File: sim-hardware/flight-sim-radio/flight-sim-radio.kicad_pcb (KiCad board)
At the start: 2 copper layers, 180.5 x 50 mm, 22 parts, among them J1 Conn_01x04, J2 Conn_01x03, J3 Conn_01x08, SW1 SW_Push, SW2 SW_Rotary_1x7_MP, SW3 RotaryEncoder_Switch, SW4 RotaryEncoder_Switch, U1 74LS148, U4 TM1637, U5 TM1637

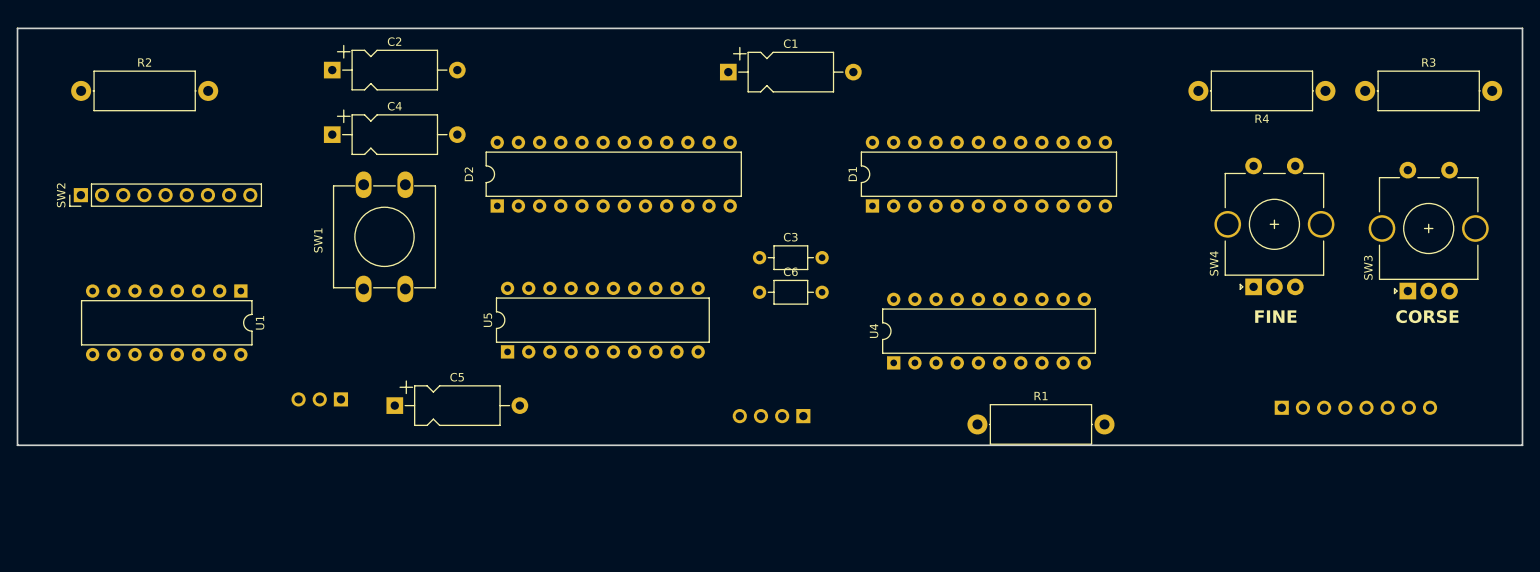
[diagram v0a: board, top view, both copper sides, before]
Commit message: 7 Segment Models created
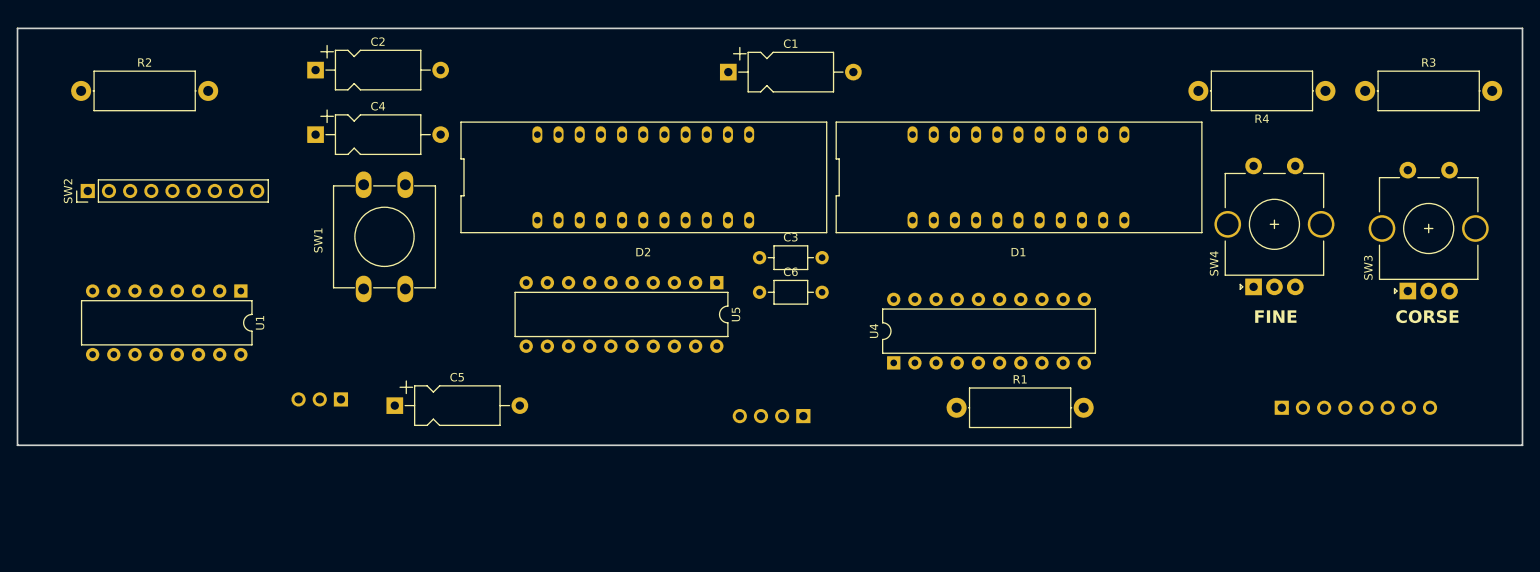
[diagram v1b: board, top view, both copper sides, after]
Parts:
- D1, D2: footprint Package_DIP:DIP-24_W7.62mm -> radio_footprints:FJ3661AH-DIP22
- moved U5 26.4 mm to (158.6, 118.0), turned to -90 degrees
- moved D1 17.8 mm to (194.8, 105.4), turned to 0 degrees
- moved D2 17.8 mm to (149.8, 105.4), turned to 0 degrees
- moved R1 3.20 mm to (187.4, 133.0)
- moved C2 2.00 mm to (110.5, 92.5)
- moved C4 2.00 mm to (110.5, 100.2)
- moved SW2 0.97 mm to (83.2, 107.0)

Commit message: More PCB updates
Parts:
- moved R2 150.4 mm to (232.8, 90.5)
- moved SW2 147.7 mm to (230.8, 102.0)
- moved U1 144.6 mm to (246.1, 121.9)
- moved SW1 97.3 mm to (213.5, 114.0)
- moved U5 72.5 mm to (86.2, 121.2), turned to 90 degrees
- moved SW3 66.2 mm to (175.5, 114.5)
- moved J2 61.0 mm to (174.5, 131.5)
- moved J1 52.0 mm to (117.0, 134.0)
- moved D1 50.3 mm to (144.5, 103.5)
- moved D2 50.3 mm to (99.5, 103.5)
- moved U4 50.3 mm to (129.6, 125.8)
- moved C1 50.3 mm to (109.7, 90.9)
- moved C6 50.3 mm to (113.5, 117.3)
- moved C3 50.3 mm to (113.5, 113.2)
- moved R1 50.3 mm to (137.1, 131.2)
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
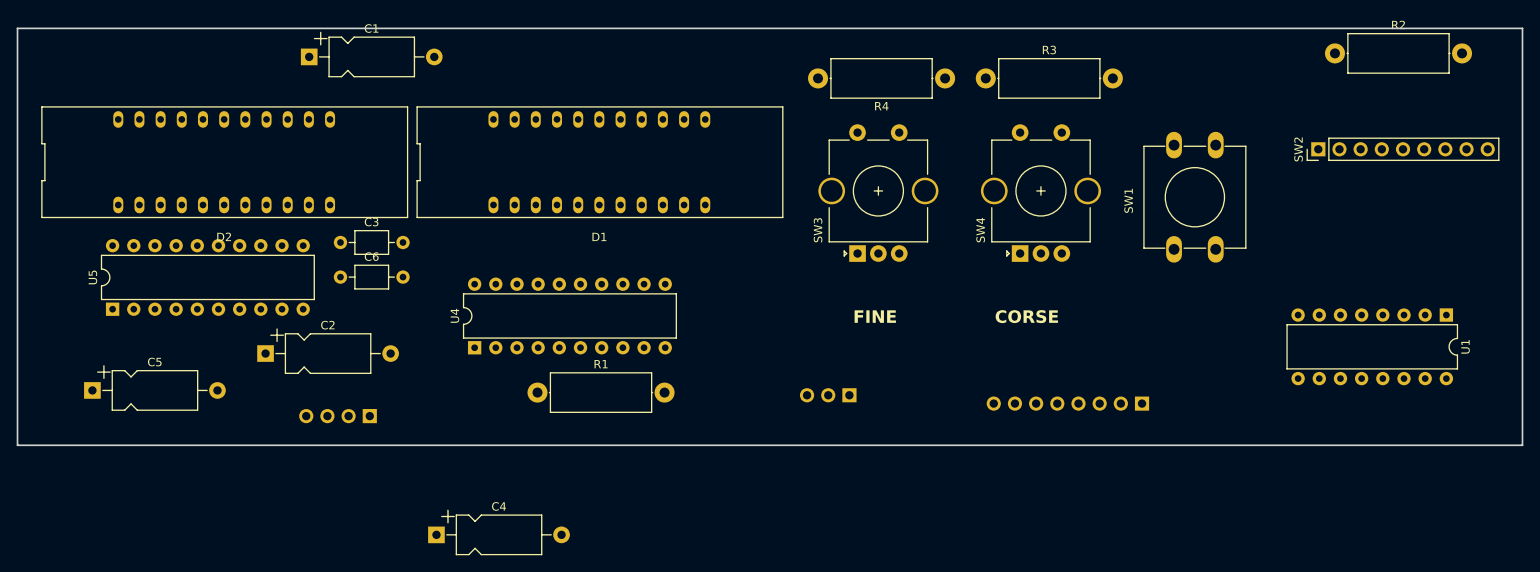
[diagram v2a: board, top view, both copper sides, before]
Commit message: input layed out
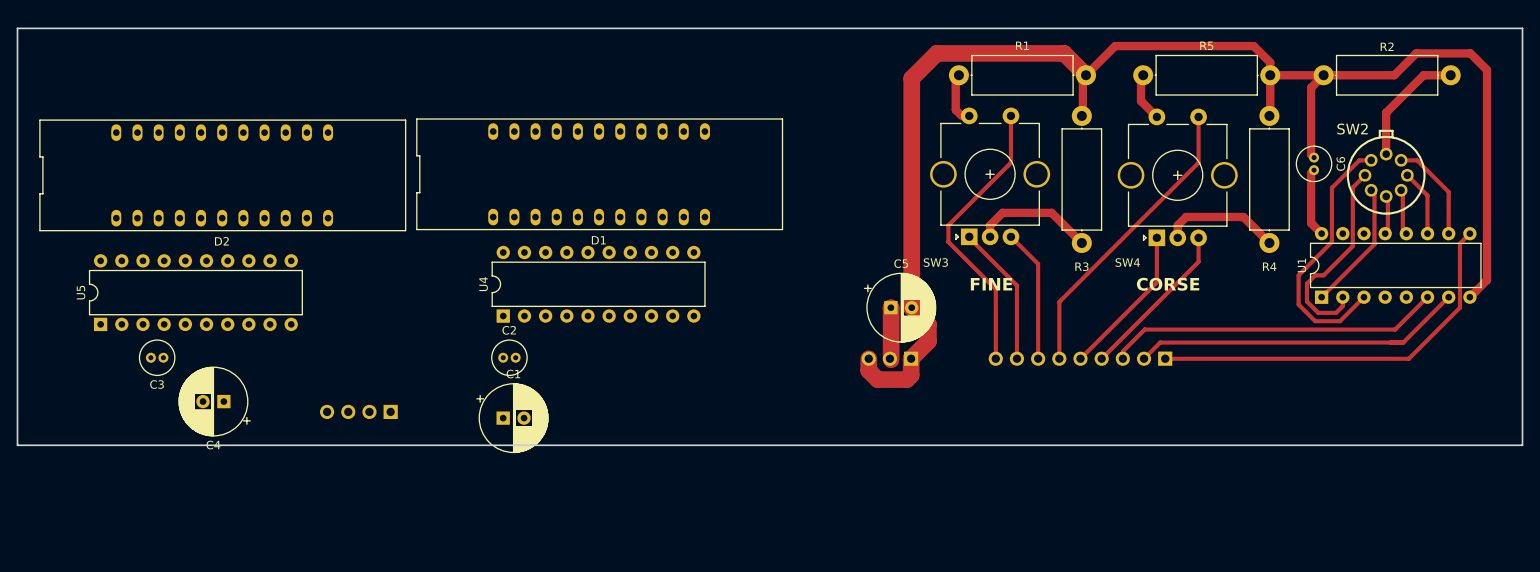
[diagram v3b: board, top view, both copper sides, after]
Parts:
- removed J3: Conn_01x08, Connector_PinHeader_2.54mm:PinHeader_1x08_P2.54mm_Vertical
- removed SW1: SW_Push, Button_Switch_THT:SW_PUSH-12mm
- added J4: Conn_01x09, Connector_PinHeader_2.54mm:PinHeader_1x09_P2.54mm_Vertical, B.Cu at (212.4, 127.1)
- added R5: 1k, Resistor_THT:R_Axial_DIN0414_L11.9mm_D4.5mm_P15.24mm_Horizontal, F.Cu at (225.0, 93.1)
- C1, C4, C5: footprint Capacitor_THT:CP_Axial_L10.0mm_D4.5mm_P15.00mm_Horizontal -> Capacitor_THT:CP_Radial_D8.0mm_P2.50mm
- C2: footprint Capacitor_THT:CP_Axial_L10.0mm_D4.5mm_P15.00mm_Horizontal -> Capacitor_THT:C_Radial_D4.0mm_H5.0mm_P1.50mm
- C3, C6: footprint Capacitor_THT:C_Axial_L3.8mm_D2.6mm_P7.50mm_Horizontal -> Capacitor_THT:C_Radial_D4.0mm_H5.0mm_P1.50mm
- SW2: value SW_Rotary_1x7_MP -> RS-08 300±150GF; footprint Connector_PinHeader_2.54mm:PinHeader_1x09_P2.54mm_Vertical -> radio_footprints:SW-TH_RS-08-300-150GF
- moved C6 117.6 mm to (230.2, 103.0), turned to -90 degrees
- moved C5 96.3 mm to (179.5, 121.0)
- moved R1 76.0 mm to (202.9, 93.1), turned to 180 degrees
- moved C1 49.2 mm to (133.0, 134.2)
- moved R4 39.2 mm to (224.9, 98.0), turned to -90 degrees
- moved C4 30.1 mm to (99.5, 132.3), turned to 180 degrees
- moved C2 28.5 mm to (133.0, 127.0)
- moved C3 25.3 mm to (92.2, 127.0), turned to 180 degrees
- moved SW4 16.5 mm to (211.4, 112.6)
- moved U1 15.1 mm to (231.2, 119.7), turned to 90 degrees
- moved SW3 13.5 mm to (188.9, 112.5)
- moved R3 12.4 mm to (202.4, 98.0), turned to -90 degrees
- moved SW2 8.72 mm to (238.9, 105.1), turned to 0 degrees
- moved J2 8.60 mm to (181.9, 127.1)
- moved U4 5.12 mm to (133.0, 122.0)
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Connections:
- R1 pad 1: Net-(R1-Pad1) -> GND
- R1 pad 2: /button_1 -> Net-(R1-Pad2)
- SW3 pad S1: unconnected-(SW3-PadS1) -> /BUTTON_2
- SW3 pad S2: unconnected-(SW3-PadS2) -> Net-(R1-Pad2)
- SW4 pad S1: unconnected-(SW4-PadS1) -> /BUTTON_1
- SW4 pad S2: unconnected-(SW4-PadS2) -> Net-(R5-Pad2)
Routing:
- net GND: track 0.00 -> 170.6 mm
- net /RSWO_1: track 0.00 -> 47.3 mm
- net /RSWO_2: track 0.00 -> 41.2 mm
- net /RSWO_3: track 0.00 -> 40.1 mm
- net /BUTTON_1: track 0.00 -> 35.9 mm
- net /BUTTON_2: track 0.00 -> 34.6 mm
- net /RSW_7: track 0.00 -> 31.6 mm
- net /RSW_6: track 0.00 -> 24.9 mm
- net /rotaryEI_B: track 0.00 -> 19.3 mm
- net /rotaryEI_A: track 0.00 -> 18.3 mm
- net /rotaryEO_A: track 0.00 -> 17.0 mm
- net /rotaryEO_B: track 0.00 -> 16.0 mm
- net /RSW_5: track 0.00 -> 15.6 mm
- net Net-(R2-Pad2): track 0.00 -> 14.6 mm
- net VDD: track 0.00 -> 14.5 mm
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
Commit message: PCB routing done
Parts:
- moved C1 44.3 mm to (174.5, 118.9), turned to -90 degrees
- moved C2 35.1 mm to (167.2, 119.1), turned to -90 degrees
- moved C4 33.1 mm to (129.5, 118.4), turned to -90 degrees
- moved C3 31.1 mm to (122.2, 118.9), turned to -90 degrees
- moved J1 10.8 mm to (128.2, 127.1)
- moved U5 8.20 mm to (92.9, 122.9)
- moved U4 5.07 mm to (138.0, 122.9)
- moved D1 5.00 mm to (149.5, 105.1)
- moved D2 5.00 mm to (104.3, 105.3)
- moved J2 5.00 mm to (186.9, 127.1)
- moved C5 3.88 mm to (183.2, 120.0)
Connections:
- J1 pad 1: /D1_CLK -> /D1_DIO
- J1 pad 2: /D1_DIO -> /D1_CLK
- J1 pad 3: /D2_CLK -> /D2_DIO
- J1 pad 4: /D2_DIO -> /D2_CLK
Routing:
- net VDD: track 14.5 -> 195.5 mm
- net GND: track 170.6 -> 325.1 mm
- net /D1_SEG7: track 0.00 -> 53.2 mm
- net /D2_SEG7: track 0.00 -> 52.9 mm
- net /D2_DIO: track 0.00 -> 51.5 mm
- net /D2_CLK: track 0.00 -> 50.1 mm
- net /D2_SEG1: track 0.00 -> 38.3 mm
- net /D1_SEG1: track 0.00 -> 38.1 mm
- net /D2_SEG6: track 0.00 -> 34.4 mm
- net /D1_SEG6: track 0.00 -> 34.4 mm
- net /D1_SEG5: track 0.00 -> 31.7 mm
- net /D2_SEG5: track 0.00 -> 31.7 mm
- net /D1_GRID4: track 0.00 -> 31.2 mm
- net /D2_GRID4: track 0.00 -> 31.2 mm
- net /D1_GRID6: track 0.00 -> 27.3 mm
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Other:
- board size 180.5 x 50 mm -> 176 x 45.2 mm
